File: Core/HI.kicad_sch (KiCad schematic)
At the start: 17 parts, among them J4 Conn_01x10_Female, J8 Conn_01x10_Female, Q1 BSS84, Q10 BSS84, Q11 2N7002, Q12 2N7002, Q13 BSS84, Q2 BSS84, Q3 2N7002, Q4 BSS84, Q5 BSS84, Q6 2N7002, Q7 BSS84, Q8 2N7002, Q9 BSS84

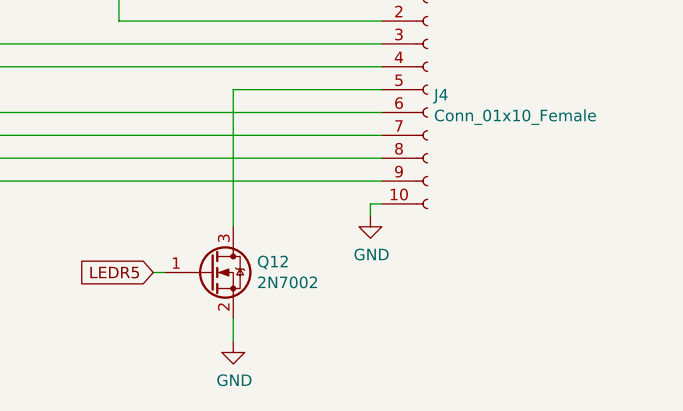
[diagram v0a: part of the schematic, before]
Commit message: Update PCBs to V3.0
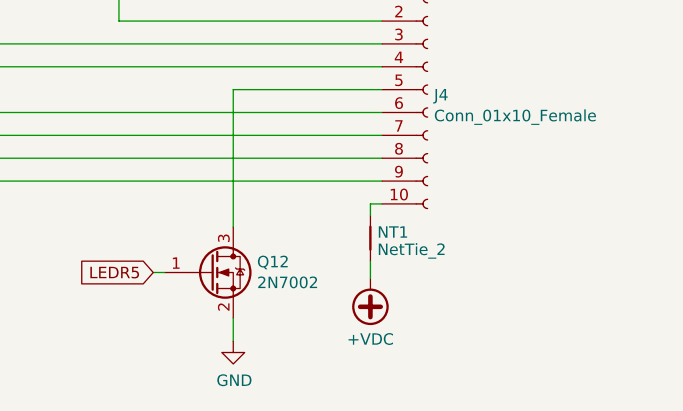
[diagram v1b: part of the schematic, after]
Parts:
- added NT1: NetTie_2, Custom_FP:NetTie_NC0603, symbol Device:NetTie_2
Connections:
- net GND: no longer J4.10 (Pin_10)
- new net: J4.10 (Pin_10), NT1.2
- new net +VDC: NT1.1
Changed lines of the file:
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@@
   (title_block
     (title "M2IDI - CV16 CORE")
-    (date "2023-04-19")
+    (date "2023-04-22")
     (rev "3.0")
     (company "GuavTek")
@@
   )
   (wire (pts (xy 208.28 45.72) (xy 208.28 38.1))
+    (stroke (width 0) (type default))
+  )
+  (wire (pts (xy 254 147.32) (xy 254 149.225))
     (stroke (width 0) (type default))
   )
@@
     )
   )
-  (symbol (lib_id "power:GND") (at 254 142.24 0) (unit 1)
-    (in_bom yes) (on_board yes) (dnp no)
-    (property "Reference" "#PWR0194" (at 254 148.59 0)
-      (effects (font (size 1.27 1.27)) hide)
-    )
-    (property "Value" "GND" (at 254.127 146.6342 0)
-      (effects (font (size 1.27 1.27)))
-    )
-    (property "Footprint" "" (at 254 142.24 0)
-      (effects (font (size 1.27 1.27)) hide)
-    )
-    (property "Datasheet" "" (at 254 142.24 0)
-      (effects (font (size 1.27 1.27)) hide)
-    )
-    (pin "1")
-    (instances
-      (project "MIDI_CV16"
-        (path "/ba515087-2175-44fd-acc2-0e447df6195b/00000000-0000-0000-0000-000060fc835e"
-          (reference "#PWR0194") (unit 1)
-        )
-      )
-    )
-  )
   (symbol (lib_id "power:GND") (at 238.76 156.21 0) (unit 1)
     (in_bom yes) (on_board yes) (dnp no)
@@
         )
       )
+    )
+  )
+  (symbol (lib_id "Device:NetTie_2") (at 254 144.78 90) (unit 1)
+    (in_bom no) (on_board yes) (dnp no) (fields_autoplaced)
+    (property "Reference" "NT1" (at 254.762 144.1363 90)
+      (effects (font (size 1.27 1.27)) (justify right))
+    )
+    (property "Value" "NetTie_2" (at 254.762 146.0573 90)
+      (effects (font (size 1.27 1.27)) (justify right))
+    )
+    (property "Footprint" "Custom_FP:NetTie_NC0603" (at 254 144.78 0)
+      (effects (font (size 1.27 1.27)) hide)
+    )
+    (property "Datasheet" "~" (at 254 144.78 0)
+      (effects (font (size 1.27 1.27)) hide)
+    )
+    (pin "1")
+    (pin "2")
+    (instances
+      (project "MIDI_CV16"
+        (path "/ba515087-2175-44fd-acc2-0e447df6195b/00000000-0000-0000-0000-000060fc835e"
+          (reference "NT1") (unit 1)
+        )
+      )
+    )
+  )
+  (symbol (lib_id "power:+VDC") (at 254 149.225 180) (unit 1)
+    (in_bom yes) (on_board yes) (dnp no) (fields_autoplaced)
+    (property "Reference" "#PWR087" (at 254 146.685 0)
+      (effects (font (size 1.27 1.27)) hide)
+    )
+    (property "Value" "+VDC" (at 254 156.0275 0)
+      (effects (font (size 1.27 1.27)))
+    )
+    (property "Footprint" "" (at 254 149.225 0)
+      (effects (font (size 1.27 1.27)) hide)
+    )
+    (property "Datasheet" "" (at 254 149.225 0)
+      (effects (font (size 1.27 1.27)) hide)
+    )
+    (pin "1")
+    (instances
+      (project "MIDI_CV16"
+        (path "/ba515087-2175-44fd-acc2-0e447df6195b/00000000-0000-0000-0000-000060fc835e"
+          (reference "#PWR087") (unit 1)
+        )
+      )

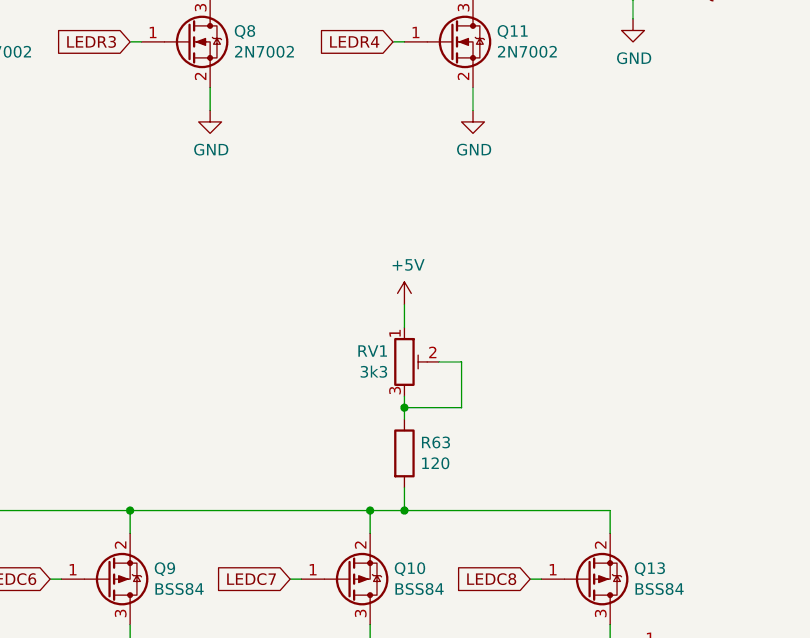
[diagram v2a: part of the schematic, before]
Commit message: Consolidate resistor values
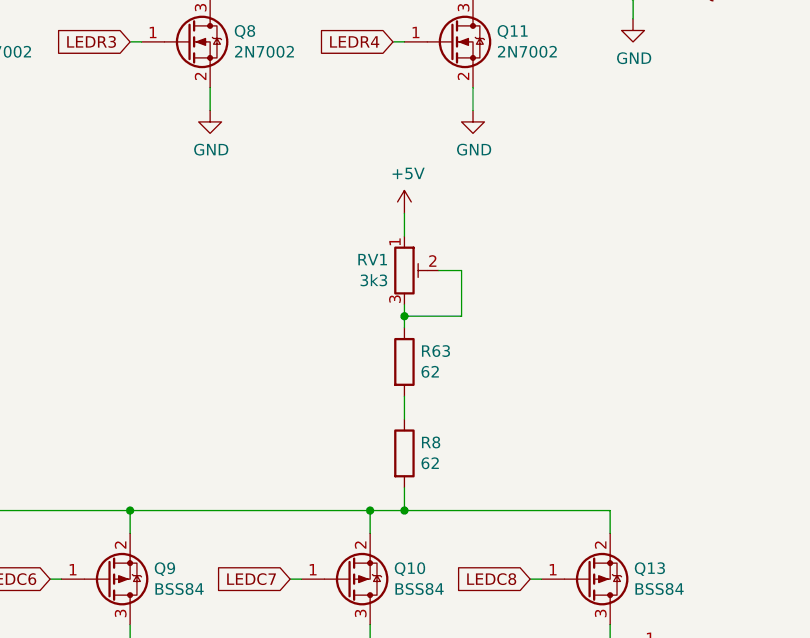
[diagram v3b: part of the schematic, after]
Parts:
- added R8: 62, Resistor_SMD:R_0603_1608Metric, symbol Device:R
- R63: value 120 -> 62
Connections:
- net at Q1.2 (S), Q10.2 (S), Q13.2 (S)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: now also R8.2; no longer R63.2
- new net: R63.2, R8.1
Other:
- moved on the sheet: R63, RV1
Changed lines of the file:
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@@
   (junction (at 92.71 102.87) (diameter 0) (color 0 0 0 0)
   )
-  (junction (at 229.87 91.44) (diameter 0) (color 0 0 0 0)
+  (junction (at 229.87 81.28) (diameter 0) (color 0 0 0 0)
   )
   (junction (at 255.27 45.72) (diameter 0) (color 0 0 0 0)
@@
     (stroke (width 0) (type default))
   )
-  (wire (pts (xy 229.87 82.55) (xy 229.87 80.01))
+  (wire (pts (xy 229.87 72.39) (xy 229.87 69.85))
+    (stroke (width 0) (type default))
+  )
+  (wire (pts (xy 229.87 90.17) (xy 229.87 92.71))
     (stroke (width 0) (type default))
   )
@@
     (stroke (width 0) (type default))
   )
-  (wire (pts (xy 236.22 91.44) (xy 229.87 91.44))
-    (stroke (width 0) (type default))
-  )
-  (wire (pts (xy 236.22 86.36) (xy 236.22 91.44))
+  (wire (pts (xy 236.22 81.28) (xy 229.87 81.28))
+    (stroke (width 0) (type default))
+  )
+  (wire (pts (xy 236.22 76.2) (xy 236.22 81.28))
     (stroke (width 0) (type default))
   )
@@
     (stroke (width 0) (type default))
   )
-  (wire (pts (xy 229.87 91.44) (xy 229.87 90.17))
+  (wire (pts (xy 229.87 81.28) (xy 229.87 80.01))
     (stroke (width 0) (type default))
   )
@@
     (stroke (width 0) (type default))
   )
-  (wire (pts (xy 233.68 86.36) (xy 236.22 86.36))
+  (wire (pts (xy 233.68 76.2) (xy 236.22 76.2))
     (stroke (width 0) (type default))
   )
@@
     (stroke (width 0) (type default))
   )
-  (wire (pts (xy 229.87 91.44) (xy 229.87 92.71))
+  (wire (pts (xy 229.87 81.28) (xy 229.87 82.55))
     (stroke (width 0) (type default))
   )
@@
     )
   )
-  (symbol (lib_id "Device:R") (at 229.87 96.52 0) (unit 1)
-    (in_bom yes) (on_board yes) (dnp no)
-    (property "Reference" "R63" (at 231.648 95.3516 0)
-      (effects (font (size 1.27 1.27)) (justify left))
-    )
-    (property "Value" "120" (at 231.648 97.663 0)
-      (effects (font (size 1.27 1.27)) (justify left))
-    )
-    (property "Footprint" "Resistor_SMD:R_0603_1608Metric" (at 228.092 96.52 90)
-      (effects (font (size 1.27 1.27)) hide)
-    )
-    (property "Datasheet" "~" (at 229.87 96.52 0)
+  (symbol (lib_id "Device:R") (at 229.87 86.36 0) (unit 1)
+    (in_bom yes) (on_board yes) (dnp no)
+    (property "Reference" "R63" (at 231.648 85.1916 0)
+      (effects (font (size 1.27 1.27)) (justify left))
+    )
+    (property "Value" "62" (at 231.648 87.503 0)
+      (effects (font (size 1.27 1.27)) (justify left))
+    )
+    (property "Footprint" "Resistor_SMD:R_0603_1608Metric" (at 228.092 86.36 90)
+      (effects (font (size 1.27 1.27)) hide)
+    )
+    (property "Datasheet" "~" (at 229.87 86.36 0)
       (effects (font (size 1.27 1.27)) hide)
     )
@@
     )
   )
-  (symbol (lib_id "Device:R_Potentiometer_Trim") (at 229.87 86.36 0) (unit 1)
-    (in_bom yes) (on_board yes) (dnp no)
-    (property "Reference" "RV1" (at 228.092 85.1916 0)
+  (symbol (lib_id "Device:R_Potentiometer_Trim") (at 229.87 76.2 0) (unit 1)
+    (in_bom yes) (on_board yes) (dnp no)
+    (property "Reference" "RV1" (at 228.092 75.0316 0)
       (effects (font (size 1.27 1.27)) (justify right))
     )
-    (property "Value" "3k3" (at 228.092 87.503 0)
+    (property "Value" "3k3" (at 228.092 77.343 0)
       (effects (font (size 1.27 1.27)) (justify right))
     )
-    (property "Footprint" "Custom_FP:VG039N" (at 229.87 86.36 0)
-      (effects (font (size 1.27 1.27)) hide)
-    )
-    (property "Datasheet" "~" (at 229.87 86.36 0)
+    (property "Footprint" "Custom_FP:VG039N" (at 229.87 76.2 0)
+      (effects (font (size 1.27 1.27)) hide)
+    )
+    (property "Datasheet" "~" (at 229.87 76.2 0)
       (effects (font (size 1.27 1.27)) hide)
     )
@@
     )
   )
-  (symbol (lib_id "power:+5V") (at 229.87 80.01 0) (unit 1)
-    (in_bom yes) (on_board yes) (dnp no)
-    (property "Reference" "#PWR0200" (at 229.87 83.82 0)
-      (effects (font (size 1.27 1.27)) hide)
-    )
-    (property "Value" "+5V" (at 230.251 75.6158 0)
+  (symbol (lib_id "power:+5V") (at 229.87 69.85 0) (unit 1)
+    (in_bom yes) (on_board yes) (dnp no)
+    (property "Reference" "#PWR0200" (at 229.87 73.66 0)
+      (effects (font (size 1.27 1.27)) hide)
+    )
+    (property "Value" "+5V" (at 230.251 65.4558 0)
       (effects (font (size 1.27 1.27)))
     )
-    (property "Footprint" "" (at 229.87 80.01 0)
-      (effects (font (size 1.27 1.27)) hide)
-    )
-    (property "Datasheet" "" (at 229.87 80.01 0)
+    (property "Footprint" "" (at 229.87 69.85 0)
+      (effects (font (size 1.27 1.27)) hide)
+    )
+    (property "Datasheet" "" (at 229.87 69.85 0)
       (effects (font (size 1.27 1.27)) hide)
     )
@@
         )
       )
+    )
+  )
+  (symbol (lib_id "Device:R") (at 229.87 96.52 0) (unit 1)
+    (in_bom yes) (on_board yes) (dnp no)
+    (property "Reference" "R8" (at 231.648 95.3516 0)
+      (effects (font (size 1.27 1.27)) (justify left))
+    )
+    (property "Value" "62" (at 231.648 97.663 0)
+      (effects (font (size 1.27 1.27)) (justify left))
+    )
+    (property "Footprint" "Resistor_SMD:R_0603_1608Metric" (at 228.092 96.52 90)
+      (effects (font (size 1.27 1.27)) hide)
+    )
+    (property "Datasheet" "~" (at 229.87 96.52 0)
+      (effects (font (size 1.27 1.27)) hide)
+    )
+    (pin "1")
+    (pin "2")
+    (instances
+      (project "MIDI_CV16"
+        (path "/ba515087-2175-44fd-acc2-0e447df6195b/00000000-0000-0000-0000-000060fc835e"
+          (reference "R8") (unit 1)
+        )
+      )

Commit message: Finalize module
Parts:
- R63, R8: footprint Resistor_SMD:R_0603_1608Metric -> Resistor_SMD:R_0805_2012Metric
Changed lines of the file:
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@@
       (effects (font (size 1.27 1.27)) (justify left))
     )
-    (property "Footprint" "Resistor_SMD:R_0603_1608Metric" (at 228.092 86.36 90)
+    (property "Footprint" "Resistor_SMD:R_0805_2012Metric" (at 228.092 86.36 90)
       (effects (font (size 1.27 1.27)) hide)
     )
@@
       (effects (font (size 1.27 1.27)) (justify left))
     )
-    (property "Footprint" "Resistor_SMD:R_0603_1608Metric" (at 228.092 96.52 90)
-      (effects (font (size 1.27 1.27)) hide)
-    )
+    (property "Footprint" "Resistor_SMD:R_0805_2012Metric" (at 228.092 96.52 90)
+      (effects (font (size 1.27 1.27)) hide)
+    )
